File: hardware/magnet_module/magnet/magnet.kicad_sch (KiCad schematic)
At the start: 5 parts, among them U2 Leaf_Logo

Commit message: sensor design
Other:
- added sheet Extra IO (io.kicad_sch)
- sheet Load Cell ports: added 3V3, CELL{I2C}, DRDY; removed none
- sheet MCU ports: added 3V3, 5V, 5V_SERVO[0..1], BUTTON[0..1], CELL{I2C}, DRDY, GPIO0, GPIO1, PRESSURE_IN, SPARE0{I2C}, SPARE1{I2C}, STIM[0..3], TEMP{I2C}, {FDCAN}, {USB2}; removed none
- sheet Power & Data Connections ports: added 12V, 3V3, 5V, {FDCAN}, {USB2}; removed none
- sheet Sensors ports: added 3V3, PRESSURE_OUT, TEMP{I2C}; removed none

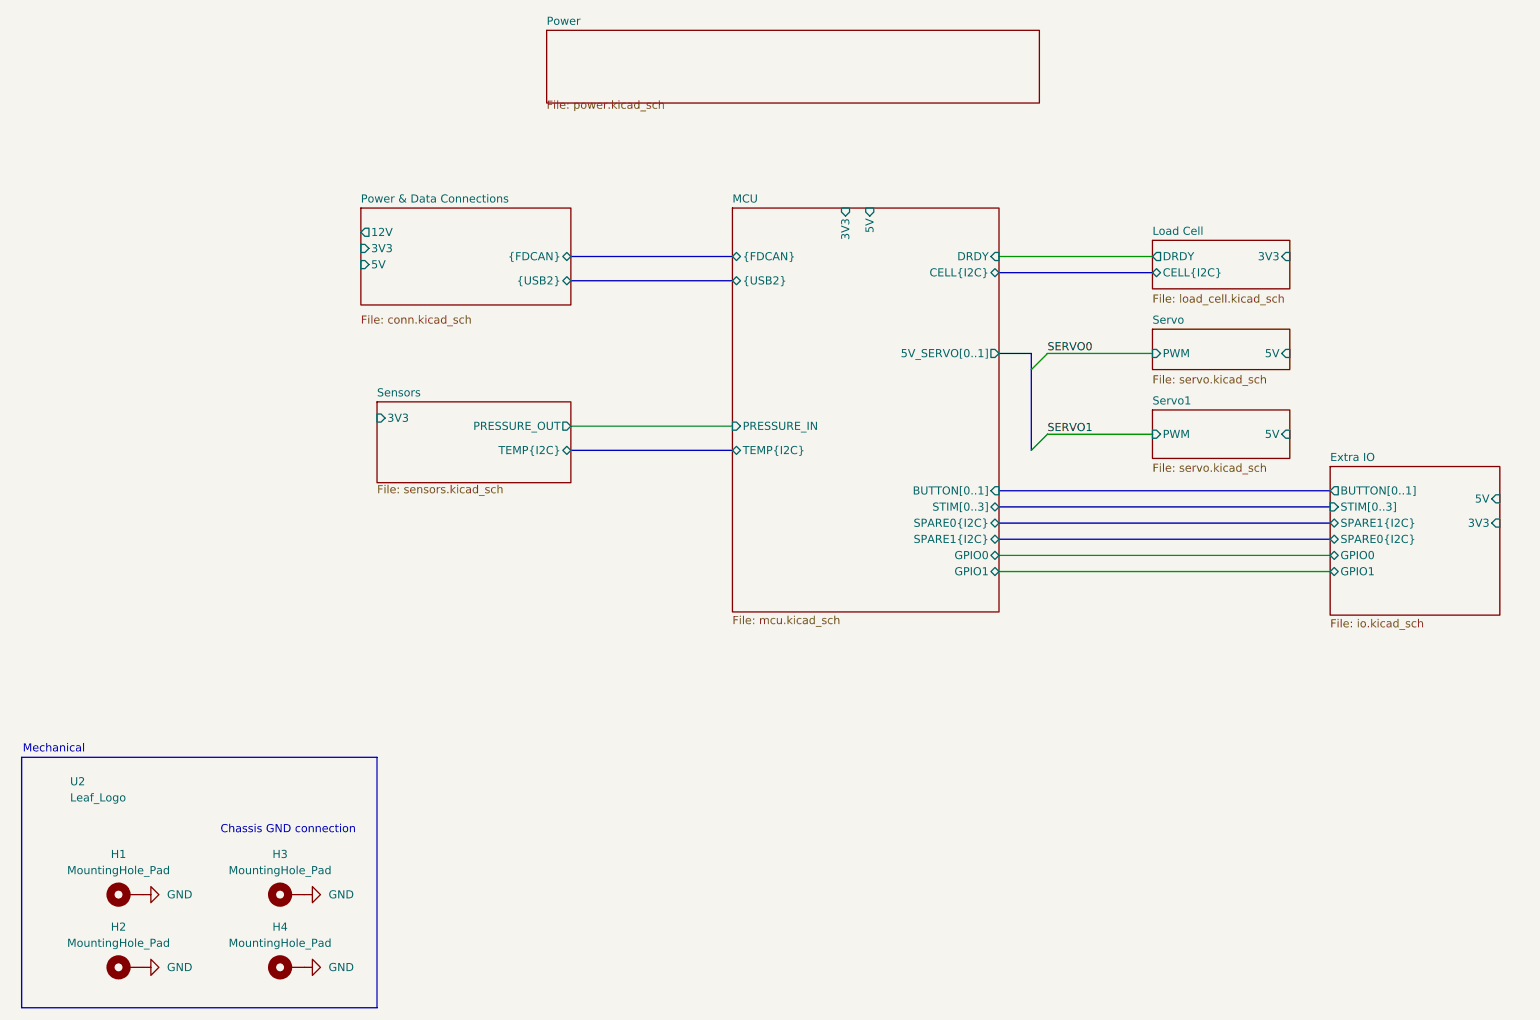
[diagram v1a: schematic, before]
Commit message: fix erc errors
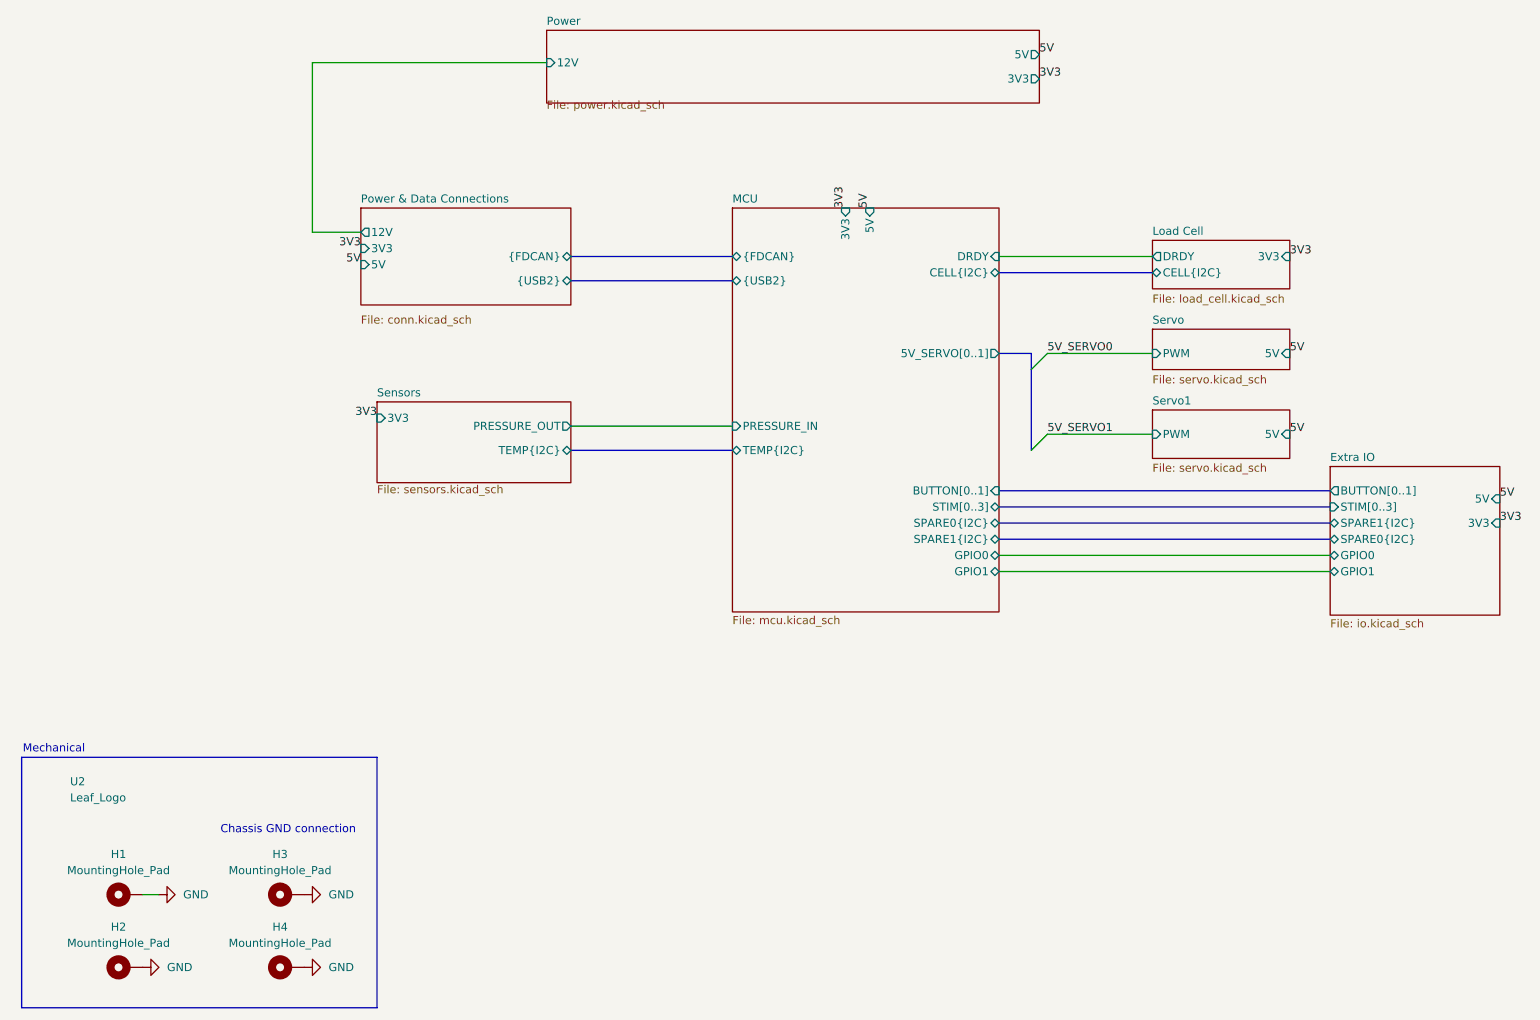
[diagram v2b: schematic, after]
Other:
- sheet Power ports: added 12V, 3V3, 5V; removed none
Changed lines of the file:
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@@
+		)
+	)
+	(wire
+		(pts
+			(xy 36.83 176.53) (xy 34.29 176.53)
+		)
+		(stroke
+			(width 0)
+			(type default)
 		)
 	)
@@
 		)
 	)
+	(wire
+		(pts
+			(xy 68.58 72.39) (xy 60.96 72.39)
+		)
+		(stroke
+			(width 0)
+			(type default)
+		)
+	)
 	(bus
 		(pts
@@
 		)
 	)
+	(wire
+		(pts
+			(xy 60.96 45.72) (xy 97.79 45.72)
+		)
+		(stroke
+			(width 0)
+			(type default)
+		)
+	)
 	(bus
 		(pts
@@
 		)
 	)
+	(wire
+		(pts
+			(xy 60.96 72.39) (xy 60.96 45.72)
+		)
+		(stroke
+			(width 0)
+			(type default)
+		)
+	)
 	(rectangle
 		(start 15.24 154.94)
@@
 		)
 	)
-	(label "SERVO0"
+	(label "5V"
+		(at 148.59 68.58 90)
+		(fields_autoplaced yes)
+		(effects
+			(font
+				(size 1.27 1.27)
+			)
+			(justify left bottom)
+		)
+	)
+	(label "5V"
+		(at 247.65 114.3 0)
+		(fields_autoplaced yes)
+		(effects
+			(font
+				(size 1.27 1.27)
+			)
+			(justify left bottom)
+		)
+	)
+	(label "5V_SERVO0"
 		(at 176.53 91.44 0)
 		(fields_autoplaced yes)
@@
 		)
 	)
-	(label "SERVO1"
+	(label "5V"
+		(at 214.63 91.44 0)
+		(fields_autoplaced yes)
+		(effects
+			(font
+				(size 1.27 1.27)
+			)
+			(justify left bottom)
+		)
+	)
+	(label "3V3"
+		(at 214.63 76.2 0)
+		(fields_autoplaced yes)
+		(effects
+			(font
+				(size 1.27 1.27)
+			)
+			(justify left bottom)
+		)
+	)
+	(label "5V"
+		(at 175.26 44.45 0)
+		(fields_autoplaced yes)
+		(effects
+			(font
+				(size 1.27 1.27)
+			)
+			(justify left bottom)
+		)
+	)
+	(label "3V3"
+		(at 144.78 68.58 90)
+		(fields_autoplaced yes)
+		(effects
+			(font
+				(size 1.27 1.27)
+			)
+			(justify left bottom)
+		)
+	)
+	(label "5V"
+		(at 68.58 77.47 180)
+		(fields_autoplaced yes)
+		(effects
+			(font
+				(size 1.27 1.27)
+			)
+			(justify right bottom)
+		)
+	)
+	(label "3V3"
+		(at 68.58 74.93 180)
+		(fields_autoplaced yes)
+		(effects
+			(font
+				(size 1.27 1.27)
+			)
+			(justify right bottom)
+		)
+	)
+	(label "3V3"
+		(at 175.26 48.26 0)
+		(fields_autoplaced yes)
+		(effects
+			(font
+				(size 1.27 1.27)
+			)
+			(justify left bottom)
+		)
+	)
+	(label "5V_SERVO1"
 		(at 176.53 104.14 0)
 		(fields_autoplaced yes)
@@
 		)
 	)
-	(symbol
-		(lib_id "power:GND")
-		(at 34.29 176.53 90)
-		(unit 1)
-		(exclude_from_sim no)
-		(in_bom yes)
-		(on_board yes)
-		(dnp no)
-		(fields_autoplaced yes)
-		(property "Reference" "#PWR07"
-			(at 40.64 176.53 0)
-			(effects
-				(font
-					(size 1.27 1.27)
-				)
-				(hide yes)
-			)
-		)
-		(property "Value" "GND"
-			(at 38.1 176.5299 90)
-			(effects
-				(font
-					(size 1.27 1.27)
-				)
-				(justify right)
-			)
-		)
-		(property "Footprint" ""
-			(at 34.29 176.53 0)
-			(effects
-				(font
-					(size 1.27 1.27)
-				)
-				(hide yes)
-			)
-		)
-		(property "Datasheet" ""
-			(at 34.29 176.53 0)
-			(effects
-				(font
-					(size 1.27 1.27)
-				)
-				(hide yes)
-			)
-		)
-		(property "Description" "Power symbol creates a global label with name \"GND\" , ground"
-			(at 34.29 176.53 0)
-			(effects
-				(font
-					(size 1.27 1.27)
-				)
-				(hide yes)
-			)
-		)
-		(pin "1"
-		)
-		(instances
-			(project "magnet"
-				(path "/aa5044b8-67cd-4b5a-a593-0df9431eb095"
-					(reference "#PWR07")
-					(unit 1)
-				)
-			)
+	(label "3V3"
+		(at 71.12 101.6 180)
+		(fields_autoplaced yes)
+		(effects
+			(font
+				(size 1.27 1.27)
+			)
+			(justify right bottom)
+		)
+	)
+	(label "5V"
+		(at 214.63 104.14 0)
+		(fields_autoplaced yes)
+		(effects
+			(font
+				(size 1.27 1.27)
+			)
+			(justify left bottom)
+		)
+	)
+	(label "3V3"
+		(at 247.65 118.11 0)
+		(fields_autoplaced yes)
+		(effects
+			(font
+				(size 1.27 1.27)
+			)
+			(justify left bottom)
 		)
 	)
@@
 	)
 	(symbol
+		(lib_id "power:GND")
+		(at 36.83 176.53 90)
+		(unit 1)
+		(exclude_from_sim no)
+		(in_bom yes)
+		(on_board yes)
+		(dnp no)
+		(fields_autoplaced yes)
+		(property "Reference" "#PWR07"
+			(at 43.18 176.53 0)
+			(effects
+				(font
+					(size 1.27 1.27)
+				)
+				(hide yes)
+			)
+		)
+		(property "Value" "GND"
+			(at 40.64 176.5299 90)
+			(effects
+				(font
+					(size 1.27 1.27)
+				)
+				(justify right)
+			)
+		)
+		(property "Footprint" ""
+			(at 36.83 176.53 0)
+			(effects
+				(font
+					(size 1.27 1.27)
+				)
+				(hide yes)
+			)
+		)
+		(property "Datasheet" ""
+			(at 36.83 176.53 0)
+			(effects
+				(font
+					(size 1.27 1.27)
+				)
+				(hide yes)
+			)
+		)
+		(property "Description" "Power symbol creates a global label with name \"GND\" , ground"
+			(at 36.83 176.53 0)
+			(effects
+				(font
+					(size 1.27 1.27)
+				)
+				(hide yes)
+			)
+		)
+		(pin "1"
+		)
+		(instances
+			(project ""
+				(path "/aa5044b8-67cd-4b5a-a593-0df9431eb095"
+					(reference "#PWR07")
+					(unit 1)
+				)
+			)
+		)
+	)
+	(symbol
 		(lib_id "Mechanical:MountingHole_Pad")
 		(at 31.75 187.96 90)
@@
 			)
 		)
+		(pin "5V" output
+			(at 175.26 44.45 0)
+			(effects
+				(font
+					(size 1.27 1.27)
+				)
+				(justify right)
+			)
+		)
+		(pin "3V3" output
+			(at 175.26 48.26 0)
+			(effects
+				(font
+					(size 1.27 1.27)
+				)
+				(justify right)
+			)
+		)
+		(pin "12V" input
+			(at 97.79 45.72 180)
+			(effects
+				(font
+					(size 1.27 1.27)
+				)
+				(justify left)
+			)
+		)
